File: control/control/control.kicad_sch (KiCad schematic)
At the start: 78 parts, among them J1 Molex2x15, Q1 2N3904, Q2 2N3904, Q3 2N3904, SW2 SW_SPST, U1 LM3914N

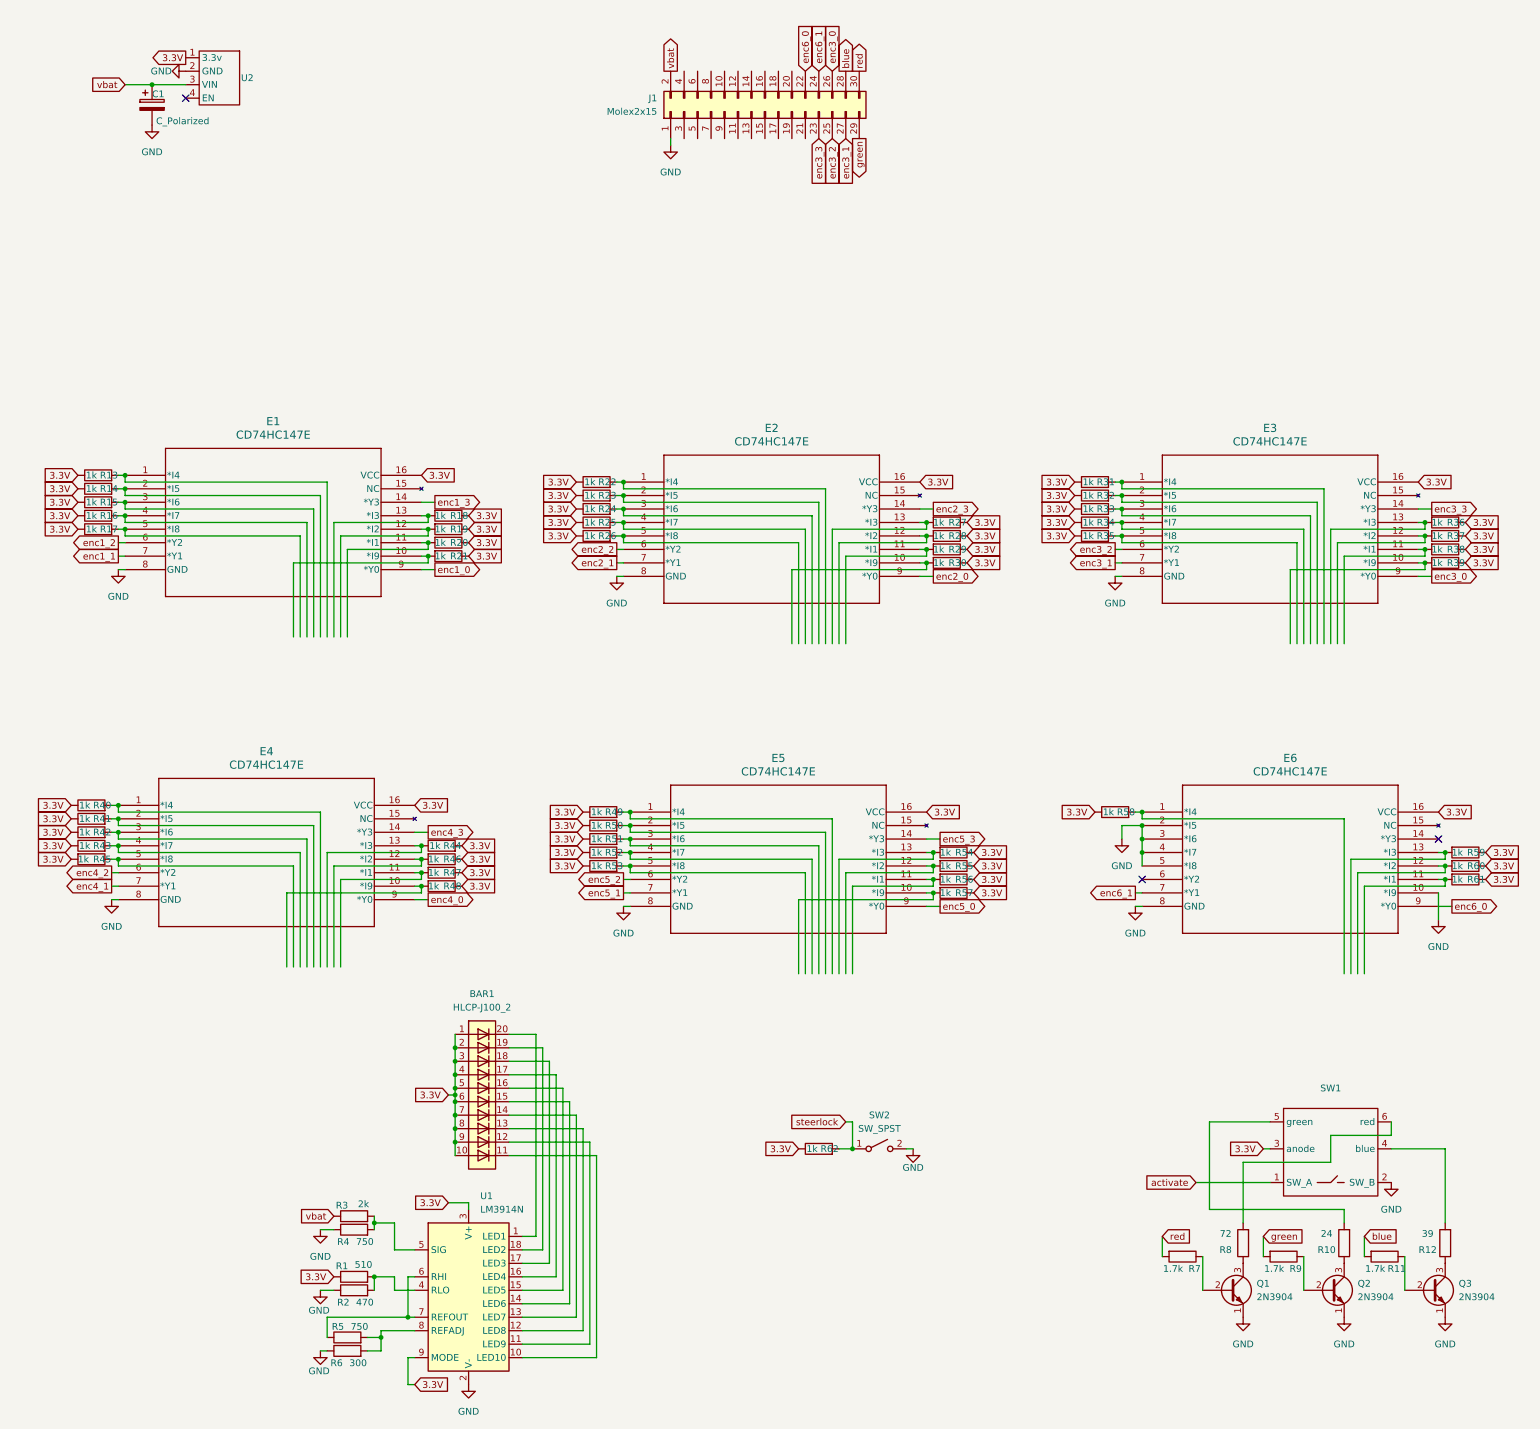
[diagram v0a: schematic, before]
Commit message: add joystick plug, adjust resistors
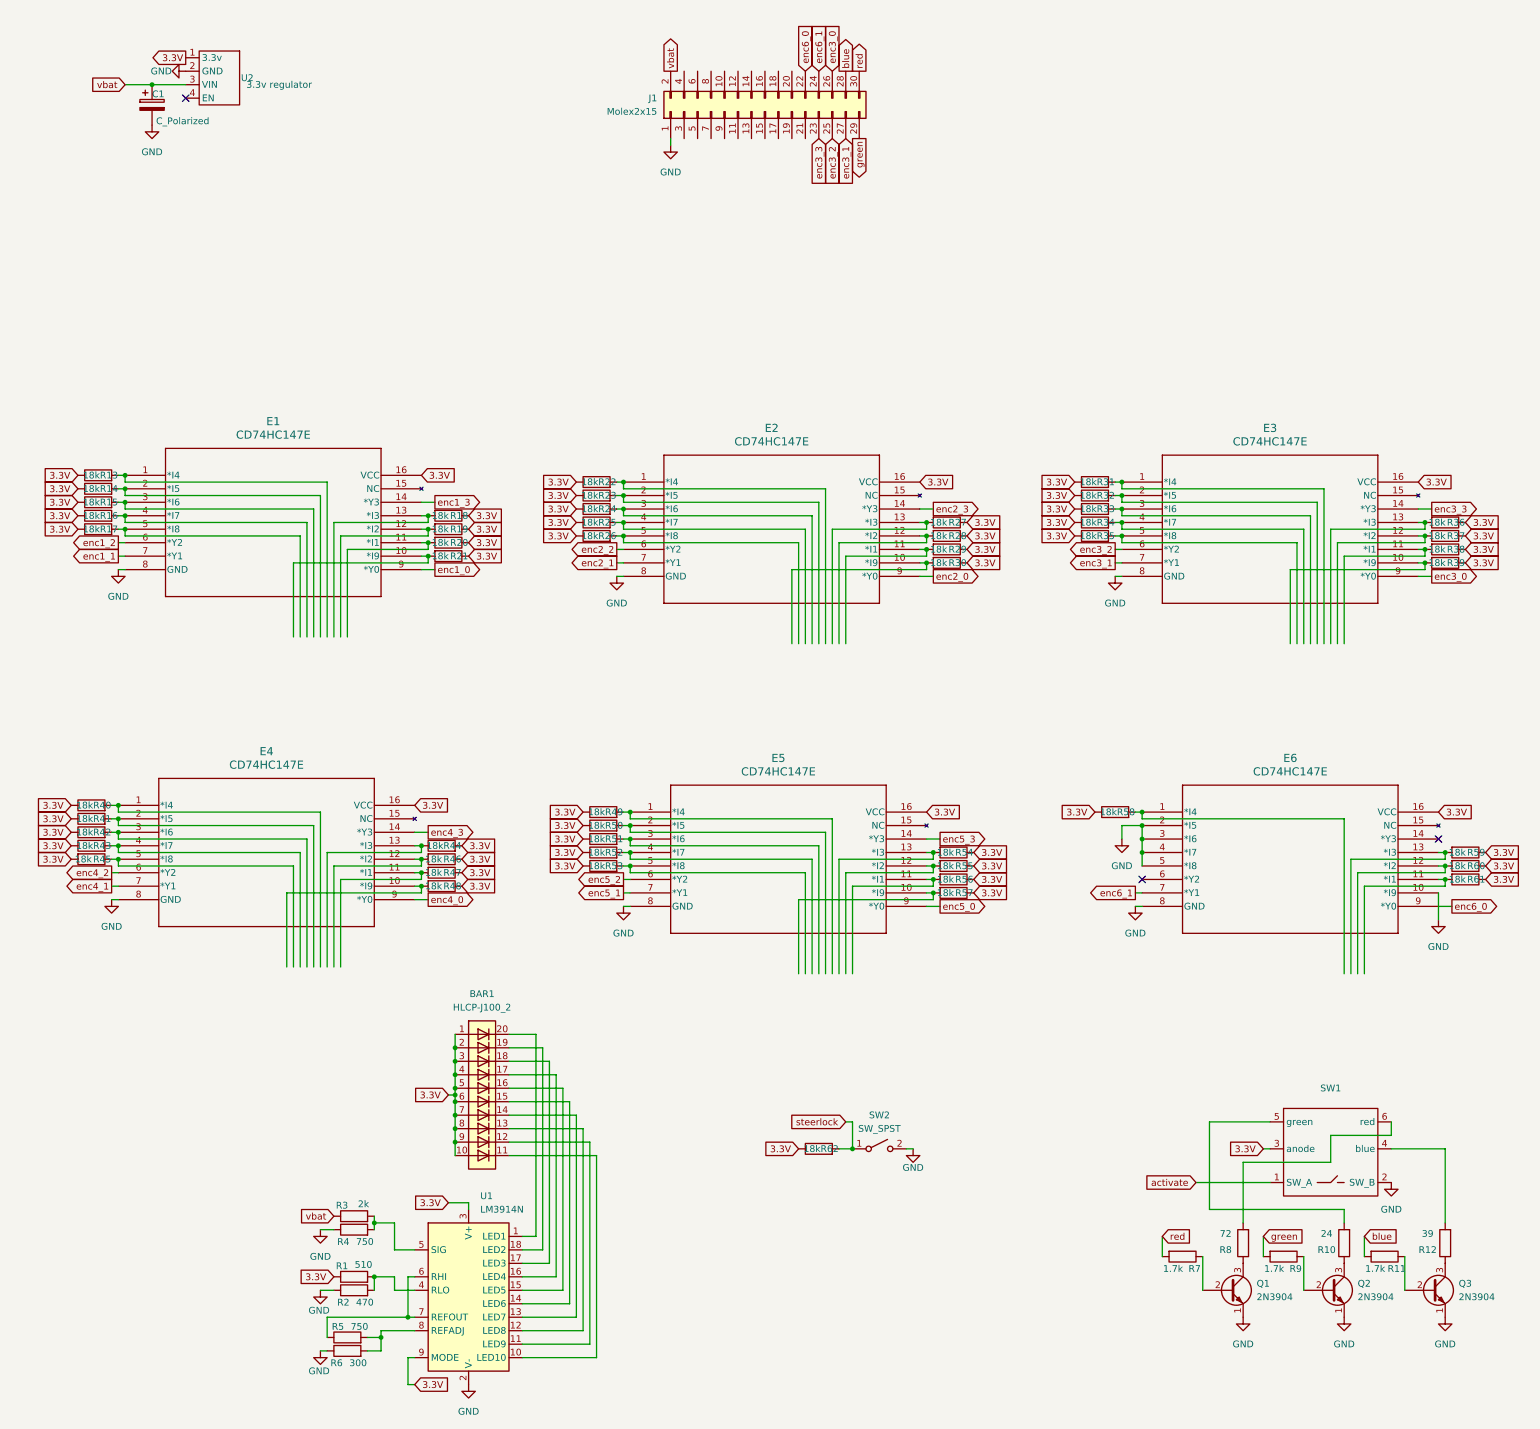
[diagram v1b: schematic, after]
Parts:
- R13, R14, R15, R16, R17, R18, R19, R20, R21, R22, R23, R24, R25, R26, R27, R28, R29, R30, R31, R32, R33, R34, R35, R36, R37, R38, R39, R40, R41, R42, R43, R44, R45, R46, R47, R48, R49, R50, R51, R52, R53, R54, R55, R56, R57, R58, R59, R60, R61, R62: value 1k -> 18k
- U2: value ~ -> 3.3v regulator
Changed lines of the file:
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@@
 			)
 		)
-		(property "Value" "1k"
+		(property "Value" "18k"
 			(at 36.83 101.6 90)
 			(effects
@@
 			)
 		)
-		(property "Value" "1k"
+		(property "Value" "18k"
 			(at 102.616 114.3 90)
 			(effects
@@
 			)
 		)
-		(property "Value" "1k"
+		(property "Value" "18k"
 			(at 130.81 110.49 90)
 			(effects
@@
 			)
 		)
-		(property "Value" "1k"
+		(property "Value" "18k"
 			(at 197.866 177.8 90)
 			(effects
@@
 			)
 		)
-		(property "Value" "1k"
+		(property "Value" "18k"
 			(at 132.08 172.72 90)
 			(effects
@@
 			)
 		)
-		(property "Value" "1k"
+		(property "Value" "18k"
 			(at 224.79 105.41 90)
 			(effects
@@
 			)
 		)
-		(property "Value" "~"
+		(property "Value" "3.3v regulator"
 			(at 66.04 27.94 90)
 			(effects
@@
 			)
 		)
-		(property "Value" "1k"
+		(property "Value" "18k"
 			(at 35.56 171.45 90)
 			(effects
@@
 			)
 		)
-		(property "Value" "1k"
+		(property "Value" "18k"
 			(at 172.72 228.6 90)
 			(effects
@@
 			)
 		)
-		(property "Value" "1k"
+		(property "Value" "18k"
 			(at 36.83 104.14 90)
 			(effects
@@
 			)
 		)
-		(property "Value" "1k"
+		(property "Value" "18k"
 			(at 224.79 113.03 90)
 			(effects
@@
 			)
 		)
-		(property "Value" "1k"
+		(property "Value" "18k"
 			(at 130.81 102.87 90)
 			(effects
@@
 			)
 		)
-		(property "Value" "1k"
+		(property "Value" "18k"
 			(at 290.576 110.49 90)
 			(effects
@@
 			)
 		)
-		(property "Value" "1k"
+		(property "Value" "18k"
 			(at 36.83 109.22 90)
 			(effects
@@
 			)
 		)
-		(property "Value" "1k"
+		(property "Value" "18k"
 			(at 102.616 116.84 90)
 			(effects
@@
 			)
 		)
-		(property "Value" "1k"
+		(property "Value" "18k"
 			(at 35.56 163.83 90)
 			(effects
@@
 			)
 		)
-		(property "Value" "1k"
+		(property "Value" "18k"
 			(at 36.83 106.68 90)
 			(effects
@@
 			)
 		)
-		(property "Value" "1k"
+		(property "Value" "18k"
 			(at 290.576 118.11 90)
 			(effects
@@
 			)
 		)
-		(property "Value" "1k"
+		(property "Value" "18k"
 			(at 101.346 179.07 90)
 			(effects
@@
 			)
 		)
-		(property "Value" "1k"
+		(property "Value" "18k"
 			(at 132.08 175.26 90)
 			(effects
@@
 			)
 		)
-		(property "Value" "1k"
+		(property "Value" "18k"
 			(at 130.81 107.95 90)
 			(effects
@@
 			)
 		)
-		(property "Value" "1k"
+		(property "Value" "18k"
 			(at 35.56 166.37 90)
 			(effects
@@
 			)
 		)
-		(property "Value" "1k"
+		(property "Value" "18k"
 			(at 196.596 115.57 90)
 			(effects
@@
 			)
 		)
-		(property "Value" "1k"
+		(property "Value" "18k"
 			(at 224.79 110.49 90)
 			(effects
@@
 			)
 		)
-		(property "Value" "1k"
+		(property "Value" "18k"
 			(at 101.6 171.45 90)
 			(effects
@@
 			)
 		)
-		(property "Value" "1k"
+		(property "Value" "18k"
 			(at 132.08 170.18 90)
 			(effects
@@
 			)
 		)
-		(property "Value" "1k"
+		(property "Value" "18k"
 			(at 36.83 111.76 90)
 			(effects
@@
 			)
 		)
-		(property "Value" "1k"
+		(property "Value" "18k"
 			(at 102.616 109.22 90)
 			(effects
@@
 			)
 		)
-		(property "Value" "1k"
+		(property "Value" "18k"
 			(at 294.386 177.8 90)
 			(effects
@@
 			)
 		)
-		(property "Value" "1k"
+		(property "Value" "18k"
 			(at 132.08 165.1 90)
 			(effects
@@
 			)
 		)
-		(property "Value" "1k"
+		(property "Value" "18k"
 			(at 290.576 115.57 90)
 			(effects
@@
 			)
 		)
-		(property "Value" "1k"
+		(property "Value" "18k"
 			(at 197.866 180.34 90)
 			(effects
@@
 			)
 		)
-		(property "Value" "1k"
+		(property "Value" "18k"
 			(at 197.866 172.72 90)
 			(effects
@@
 			)
 		)
-		(property "Value" "1k"
+		(property "Value" "18k"
 			(at 35.56 168.91 90)
 			(effects
@@
 			)
 		)
-		(property "Value" "1k"
+		(property "Value" "18k"
 			(at 290.576 113.03 90)
 			(effects
@@
 			)
 		)
-		(property "Value" "1k"
+		(property "Value" "18k"
 			(at 196.596 110.49 90)
 			(effects
@@
 			)
 		)
-		(property "Value" "1k"
+		(property "Value" "18k"
 			(at 130.81 113.03 90)
 			(effects
@@
 			)
 		)
-		(property "Value" "1k"
+		(property "Value" "18k"
 			(at 132.08 167.64 90)
 			(effects
@@
 			)
 		)
-		(property "Value" "1k"
+		(property "Value" "18k"
 			(at 196.596 113.03 90)
 			(effects
@@
 			)
 		)
-		(property "Value" "1k"
+		(property "Value" "18k"
 			(at 224.79 107.95 90)
 			(effects
@@
 			)
 		)
-		(property "Value" "1k"
+		(property "Value" "18k"
 			(at 294.386 172.72 90)
 			(effects
@@
 			)
 		)
-		(property "Value" "1k"
+		(property "Value" "18k"
 			(at 294.386 175.26 90)
 			(effects
@@
 			)
 		)
-		(property "Value" "1k"
+		(property "Value" "18k"
 			(at 101.346 176.53 90)
 			(effects
@@
 			)
 		)
-		(property "Value" "1k"
+		(property "Value" "18k"
 			(at 102.616 111.76 90)
 			(effects
@@
 			)
 		)
-		(property "Value" "1k"
+		(property "Value" "18k"
 			(at 130.81 105.41 90)
 			(effects
@@
 			)
 		)
-		(property "Value" "1k"
+		(property "Value" "18k"
 			(at 35.306 173.99 90)
 			(effects
@@
 			)
 		)
-		(property "Value" "1k"
+		(property "Value" "18k"
 			(at 224.79 102.87 90)
 			(effects
@@
 			)
 		)
-		(property "Value" "1k"
+		(property "Value" "18k"
 			(at 228.6 165.1 90)
 			(effects
@@
 			)
 		)
-		(property "Value" "1k"
+		(property "Value" "18k"
 			(at 101.346 173.99 90)
 			(effects
@@
 			)
 		)
-		(property "Value" "1k"
+		(property "Value" "18k"
 			(at 196.596 118.11 90)
 			(effects
@@
 			)
 		)
-		(property "Value" "1k"
+		(property "Value" "18k"
 			(at 197.866 175.26 90)
 			(effects

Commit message: delete binary converter chips and add different knobs
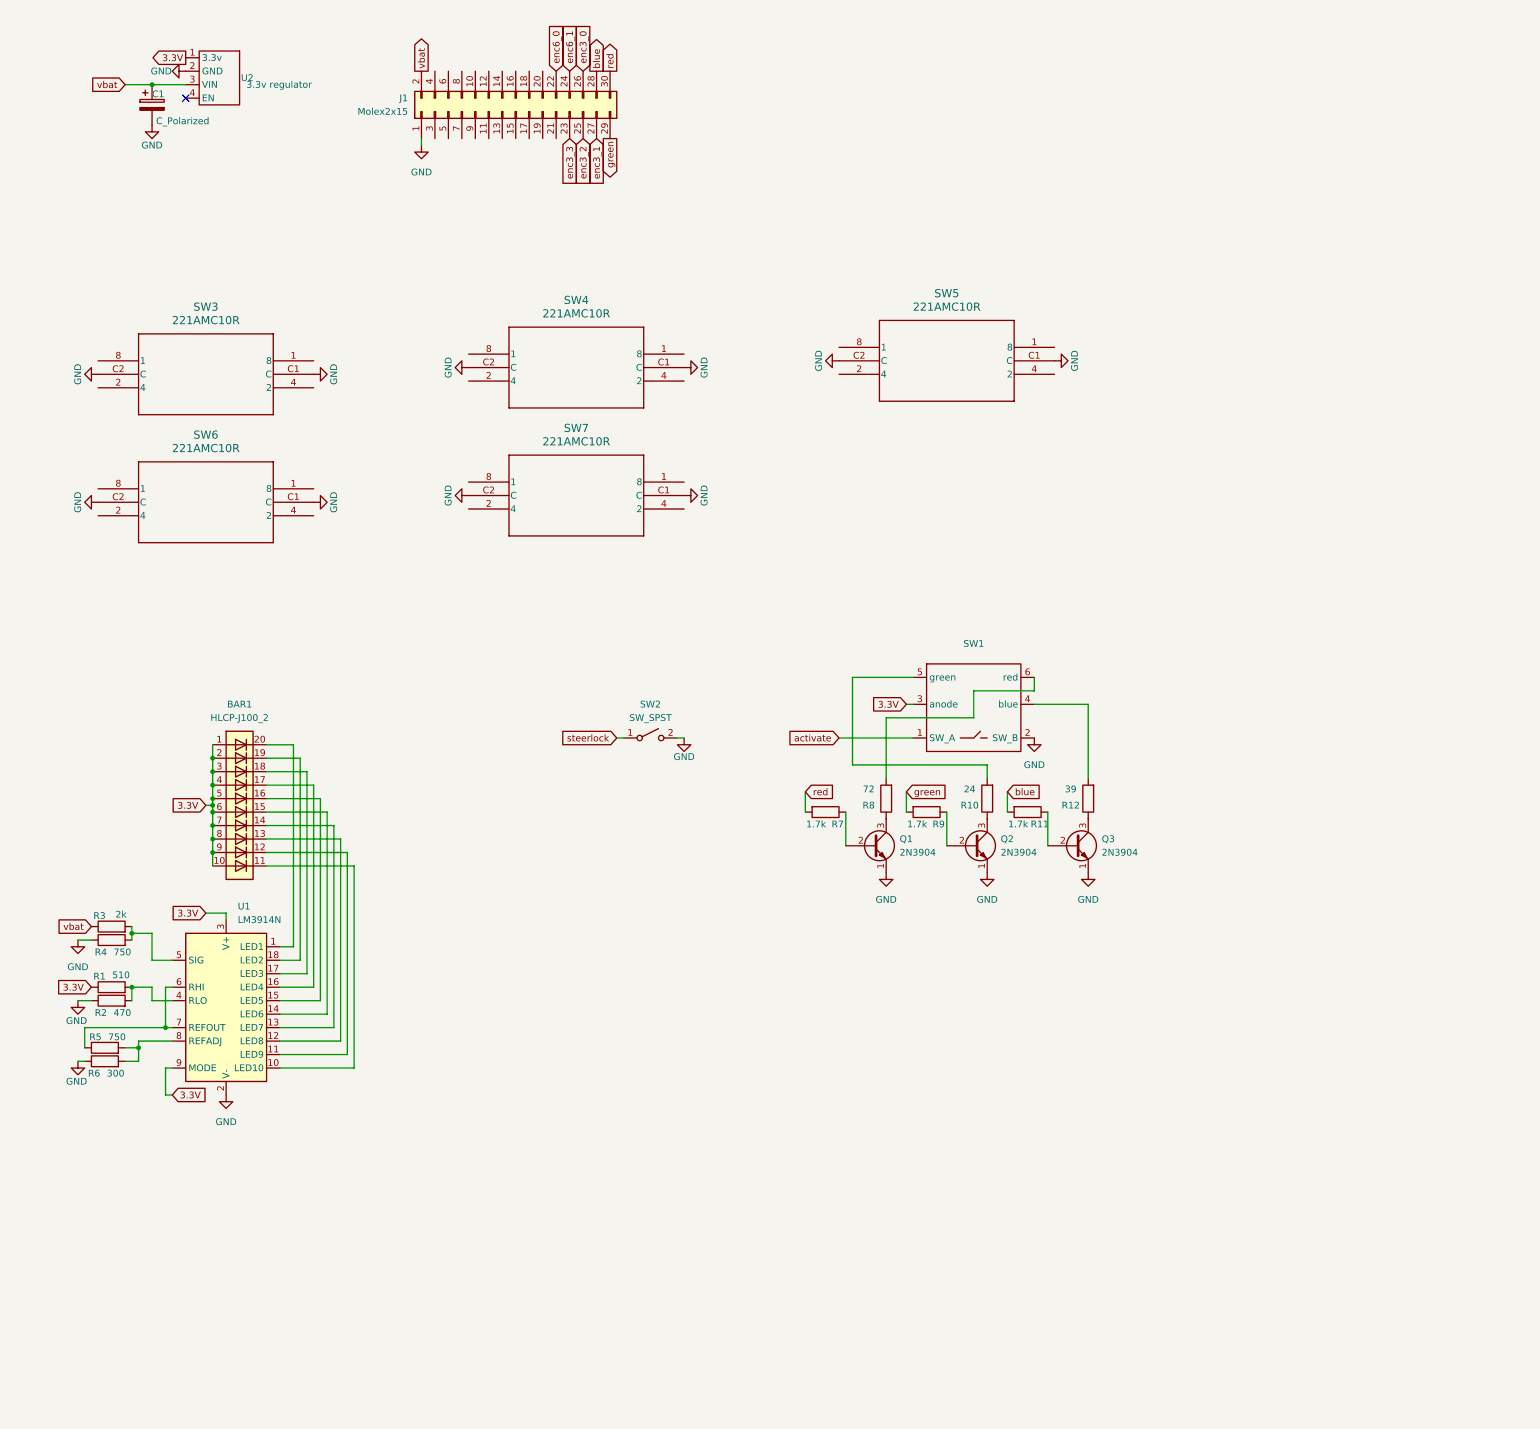
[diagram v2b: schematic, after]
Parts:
- removed E1, E2, E3, E4, E5, E6: CD74HC147E, projlib:CD74HC147E, symbol projlib:CD74HC147E
- removed R13, R14, R15, R16, R17, R18, R19, R20, R21, R22, R23, R24, R25, R26, R27, R28, R29, R30, R31, R32, R33, R34, R35, R36, R37, R38, R39, R40, R41, R42, R43, R44, R45, R46, R47, R48, R49, R50, R51, R52, R53, R54, R55, R56, R57, R58, R59, R60, R61, R62: 18k, Resistor_THT:R_Axial_DIN0204_L3.6mm_D1.6mm_P5.08mm_Horizontal, symbol Device:R
- added SW3, SW4, SW5, SW6, SW7: 221AMC10R, projlib:221ADC16, symbol projlib:221AMC10R
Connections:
- net GND: now also SW3.C1 (C), SW3.C2 (C), SW4.C1 (C), SW4.C2 (C), SW5.C1 (C), SW5.C2 (C), SW6.C1 (C), SW6.C2 (C), SW7.C1 (C), SW7.C2 (C)
- no-connect marks 3 -> 1
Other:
- moved on the sheet: BAR1, J1, Q1, Q2, Q3, R1, R10, R11, R12, R2, R3, R4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

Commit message: control pcb almost done
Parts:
- removed SW2: SW_SPST, Connector_PinHeader_2.54mm:PinHeader_1x02_P2.54mm_Vertical, symbol Switch:SW_SPST
- added R13: 2k, Resistor_THT:R_Axial_DIN0207_L6.3mm_D2.5mm_P10.16mm_Horizontal, symbol Device:R
- added S1: LP4EE1PBCTW, projlib:LP4EE1PBCTW, symbol projlib:LP4EE1PBCTW
- added U3: ~, projlib:R20405RN02Q, symbol projlib:mode switch R20405RN02Q
- Q1, Q2, Q3: footprint Package_TO_SOT_THT:TO-92_Inline -> projlib:TO-92_Inline; symbol Transistor_BJT:2N3904 -> projlib:2N3904
- SW3, SW4, SW5, SW6, SW7: value 221AMC10R -> 221ADC16
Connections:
- net enc3_1 is gone; now on net steerlock: J1.27 (Pin_27)
- net enc3_2 is gone; now on net activate: J1.25 (Pin_25)
- net enc6_0 is gone; now on an unnamed net: J1.22 (Pin_22)
- net 3.3V: now also R13.2, S1.L1 (A)
- net GND: now also S1.2 (COM_1), S1.5 (COM_2), U3.1, U3.4, U3.8
- net activate: now also R13.1
- net steerlock: now also S1.1 (NC_1)
- net vbat: no longer R3.1
- net at SW7.1 (8): now also J1.18 (Pin_18)
- net at SW7.2 (4): now also J1.15 (Pin_15)
- net at SW7.4 (2): now also J1.17 (Pin_17)
- net at SW7.8 (1): now also J1.16 (Pin_16)
- net at SW6.1 (8): now also J1.7 (Pin_7)
- net at SW6.2 (4): now also J1.5 (Pin_5)
- net at SW6.4 (2): now also J1.9 (Pin_9)
- net at SW6.8 (1): now also J1.3 (Pin_3)
- net at SW3.1 (8): now also J1.6 (Pin_6)
- net at SW3.2 (4): now also J1.8 (Pin_8)
- net at SW3.4 (2): now also J1.4 (Pin_4)
- net at SW3.8 (1): now also J1.10 (Pin_10)
- net at SW4.1 (8): now also J1.14 (Pin_14)
- net at SW4.2 (4): now also J1.11 (Pin_11)
- net at SW4.4 (2): now also J1.13 (Pin_13)
- net at SW4.8 (1): now also J1.12 (Pin_12)
- net at J1.19 (Pin_19): now also SW5.2 (4)
- net at J1.20 (Pin_20): now also SW5.8 (1)
- net at J1.21 (Pin_21): now also SW5.4 (2)
- net enc3_0: no longer names the net of J1.26 (Pin_26)
- net enc3_0: now also R3.1
- net enc3_3 renamed mode2
- net mode2: now also U3.7, U3.9
- net enc6_1 renamed mode1
- net mode1: now also U3.2, U3.3
- new net: S1.6 (NO_2), S1.L2 (K)
- no-connect marks 1 -> 6
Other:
- moved on the sheet: SW3, SW4, SW5, SW6, SW7

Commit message: final adjustments for v1.0
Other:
- company: (none) -> PNW Assistive Technology
- title: (none) -> control PCB for standing frame
- moved on the sheet: BAR1, Q1, Q2, Q3, R1, R10, R11, R12, R13, R2, R3, R4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

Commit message: v1.4
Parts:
- added NT1: NetTie_2, Jumper:SolderJumper-2_P1.3mm_Bridged_RoundedPad1.0x1.5mm, symbol Device:NetTie_2
- added R14: 0, Resistor_THT:R_Axial_DIN0207_L6.3mm_D2.5mm_P10.16mm_Horizontal, symbol Device:R
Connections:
- net 3.3V: now also NT1.1, R14.2; no longer S1.L1 (A)
- new net: NT1.2, R14.1, S1.L1 (A)
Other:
- note added: "knob1"
- note added: "knob2"
- note added: "knob3"
- note added: "knob4"
- note added: "knob5"
- note added: "mode_knob"
